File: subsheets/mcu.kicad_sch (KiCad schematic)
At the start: 16 parts, among them U3 LoRa-E5

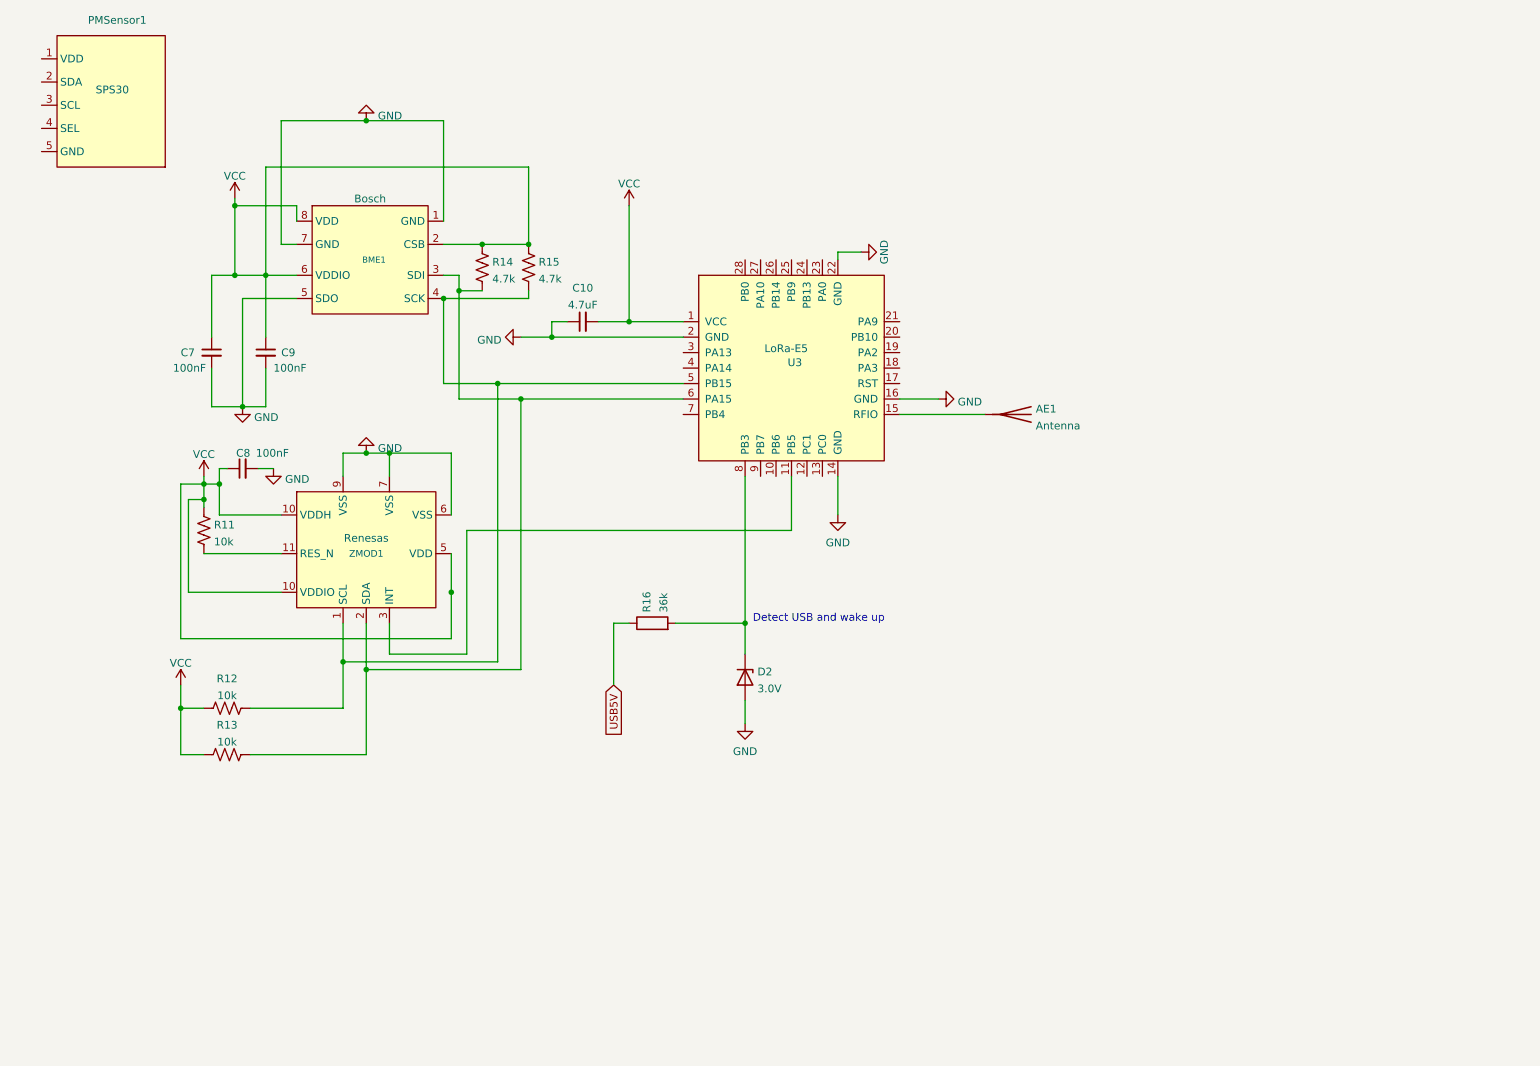
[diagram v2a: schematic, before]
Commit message: USB Comm Interface complete; Sensor and MCU connection complete;
-
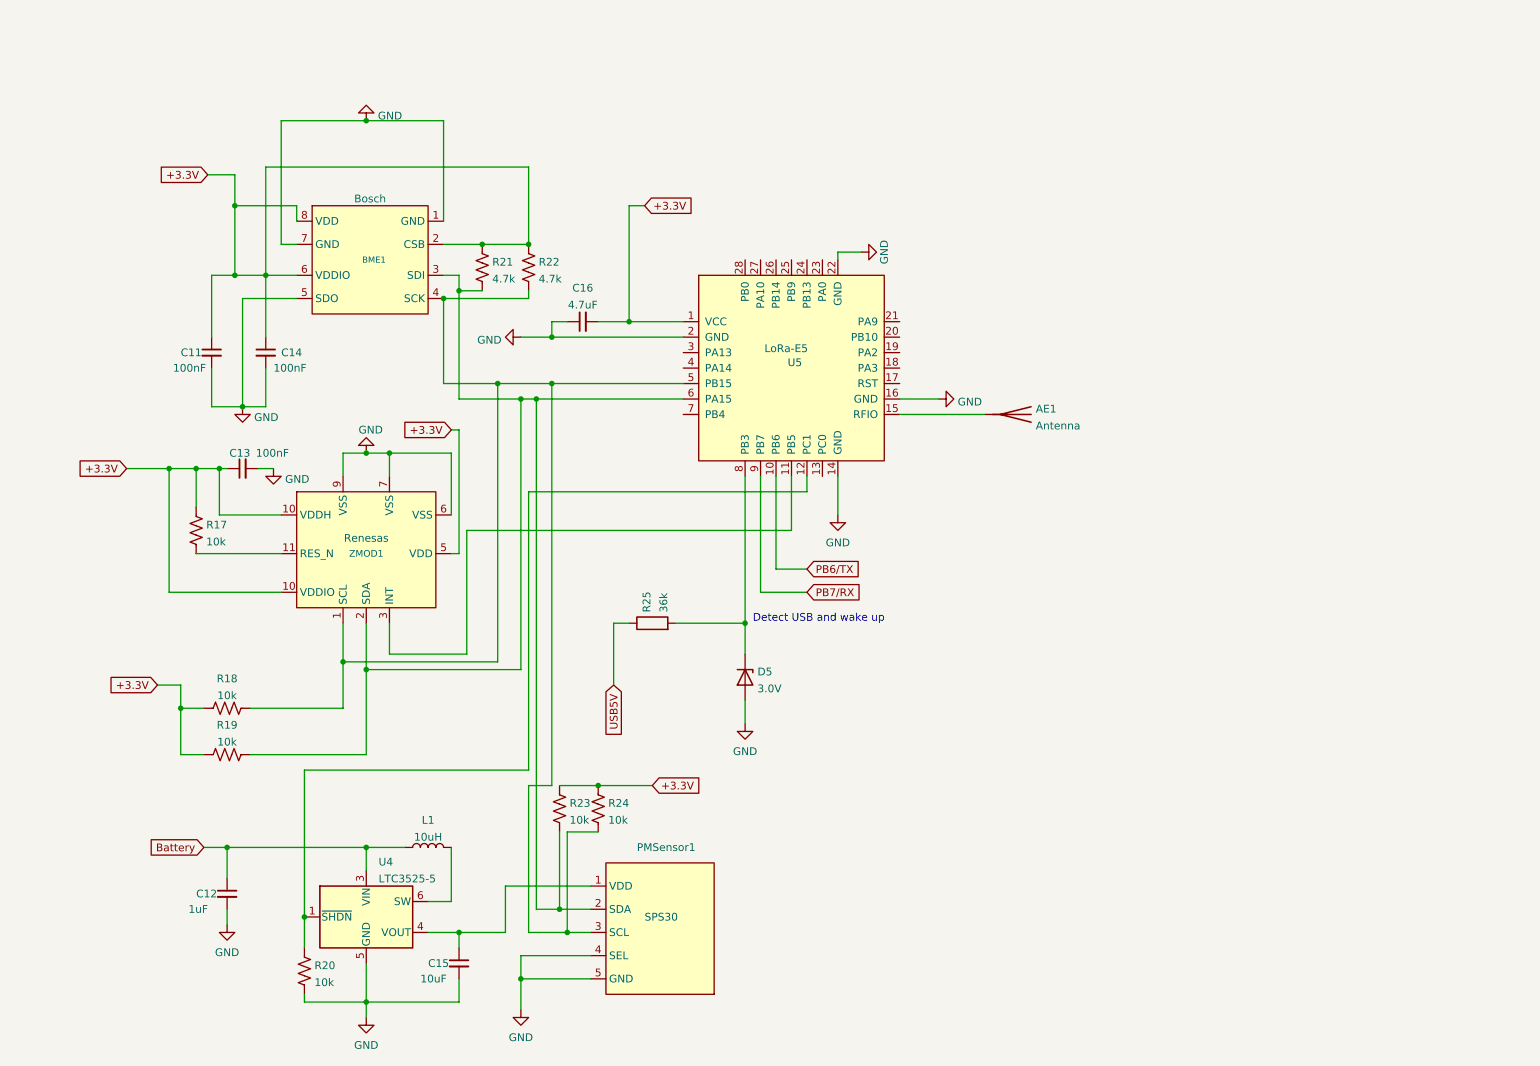
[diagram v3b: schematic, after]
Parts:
- added C12: 1uF, symbol Device:C_Small
- added C15: 10uF, symbol Device:C_Small
- added L1: 10uH, symbol Device:L
- added R20, R23, R24: 10k, symbol Device:R_US
- added U4: LTC3525-5, Package_TO_SOT_SMD:SOT-363_SC-70-6, symbol Regulator_Switching:LTC3525-5
- renumbered C7 to C11, C8 to C13, C9 to C14, C10 to C16, D2 to D5, R11 to R17, R12 to R18, R13 to R19, R14 to R21, R15 to R22, R16 to R25, U3 to U5
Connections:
- net GND: now also PMSensor1.4 (SEL), PMSensor1.5 (GND), C12.2, C15.2, R20.2, U4.2 (GND), U4.5 (GND)
- net PB6/TX: now reaches U5.10 (PB6)
- net at U5.12 (PC1): now also R20.1, U4.1 (~{SHDN})
- net at BME1.4 (SCK), R18.2, R22.2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: now also PMSensor1.3 (SCL), R24.2
- net at BME1.3 (SDI), R19.2, R21.2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: now also PMSensor1.2 (SDA), R23.2
- net PB7/RX: now reaches U5.9 (PB7)
- net at PMSensor1.1 (VDD): now also C15.1, U4.4 (VOUT)
- net VCC renamed +3.3V
- net +3.3V: now also R23.1, R24.1; no longer ZMOD1.n.c (4)
- new net: L1.2, U4.6 (SW)
- new net Battery: C12.1, L1.1, U4.3 (VIN)
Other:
- moved on the sheet: PMSensor1, R17

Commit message: A few schematic changes and fixes
-
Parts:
- removed C12: 1uF, symbol Device:C_Small
- removed C15: 10uF, symbol Device:C_Small
- removed L1: 10uH, symbol Device:L
- removed R20: 10k, symbol Device:R_US
- removed U4: LTC3525-5, Package_TO_SOT_SMD:SOT-363_SC-70-6, symbol Regulator_Switching:LTC3525-5
- renumbered C11 to C13, C13 to C14, C14 to C15, R17 to R18, R18 to R19, R19 to R20
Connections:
- net Boost SHDN/PC1: now reaches U5.12 (PC1)
- net Charge/LBO : now reaches U5.13 (PC0)
- net Charge Done: now reaches U5.20 (PB10)
- net Power On: now reaches U5.21 (PA9)
- net +5V: now reaches PMSensor1.1 (VDD)
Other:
- moved on the sheet: AE1, BME1, C13, C14, C15, C16, D5, PMSensor1, R18, R19, R20, R21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

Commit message: -
-
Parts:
- BME688: renamed from BME1; footprint Package_LGA:LGA-12_2x2mm_P0.5mm -> Package_LGA:Bosch_LGA-8_3x3mm_P0.8mm_ClockwisePinNumbering
- PMSensor1: footprint (none) -> Connector_JST:JST_EH_B5B-EH-A_1x05_P2.50mm_Vertical
- U5: footprint (none) -> LoRa-E5:LoRa-E5
- renumbered ZMOD1 to ZMOD4510

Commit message: USB updated. All footprints added for the most part
-
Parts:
- C13, C14, C15, C16: footprint (none) -> Capacitor_SMD:C_0805_2012Metric_Pad1.18x1.45mm_HandSolder
- R18, R19, R20, R21, R22, R23, R24, R25: footprint (none) -> Resistor_SMD:R_0805_2012Metric_Pad1.20x1.40mm_HandSolder

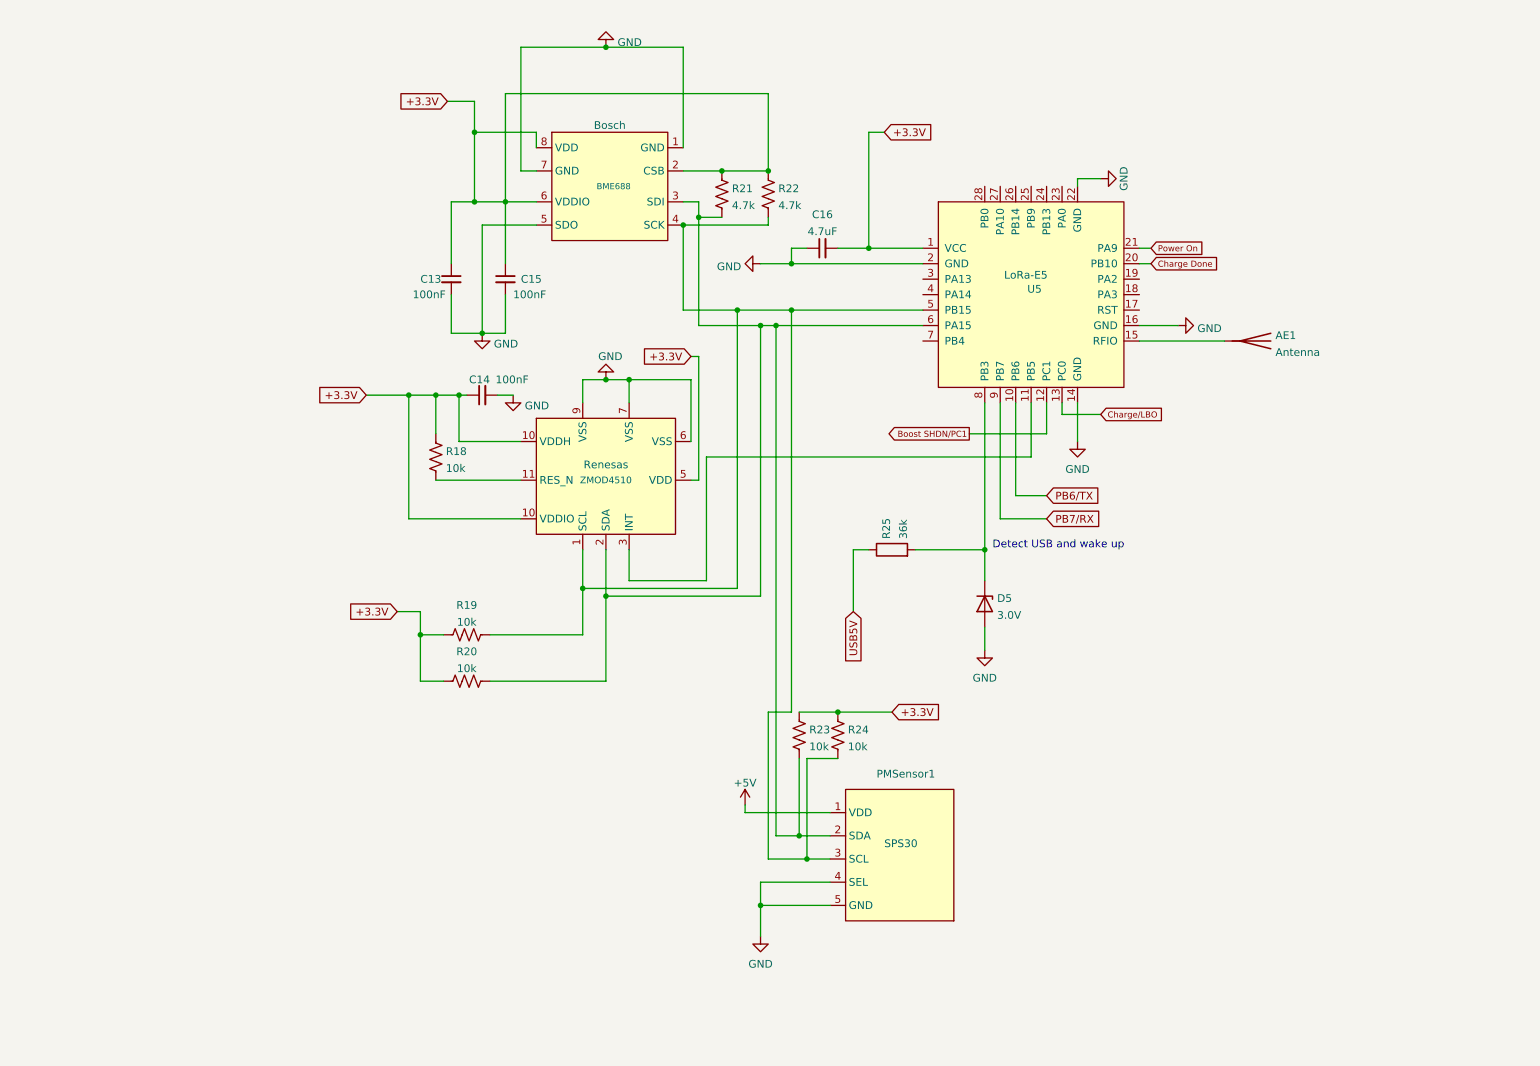
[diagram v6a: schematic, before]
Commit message: Some schematic changes. Preliminary PCB layout complete, routing not done yet
-
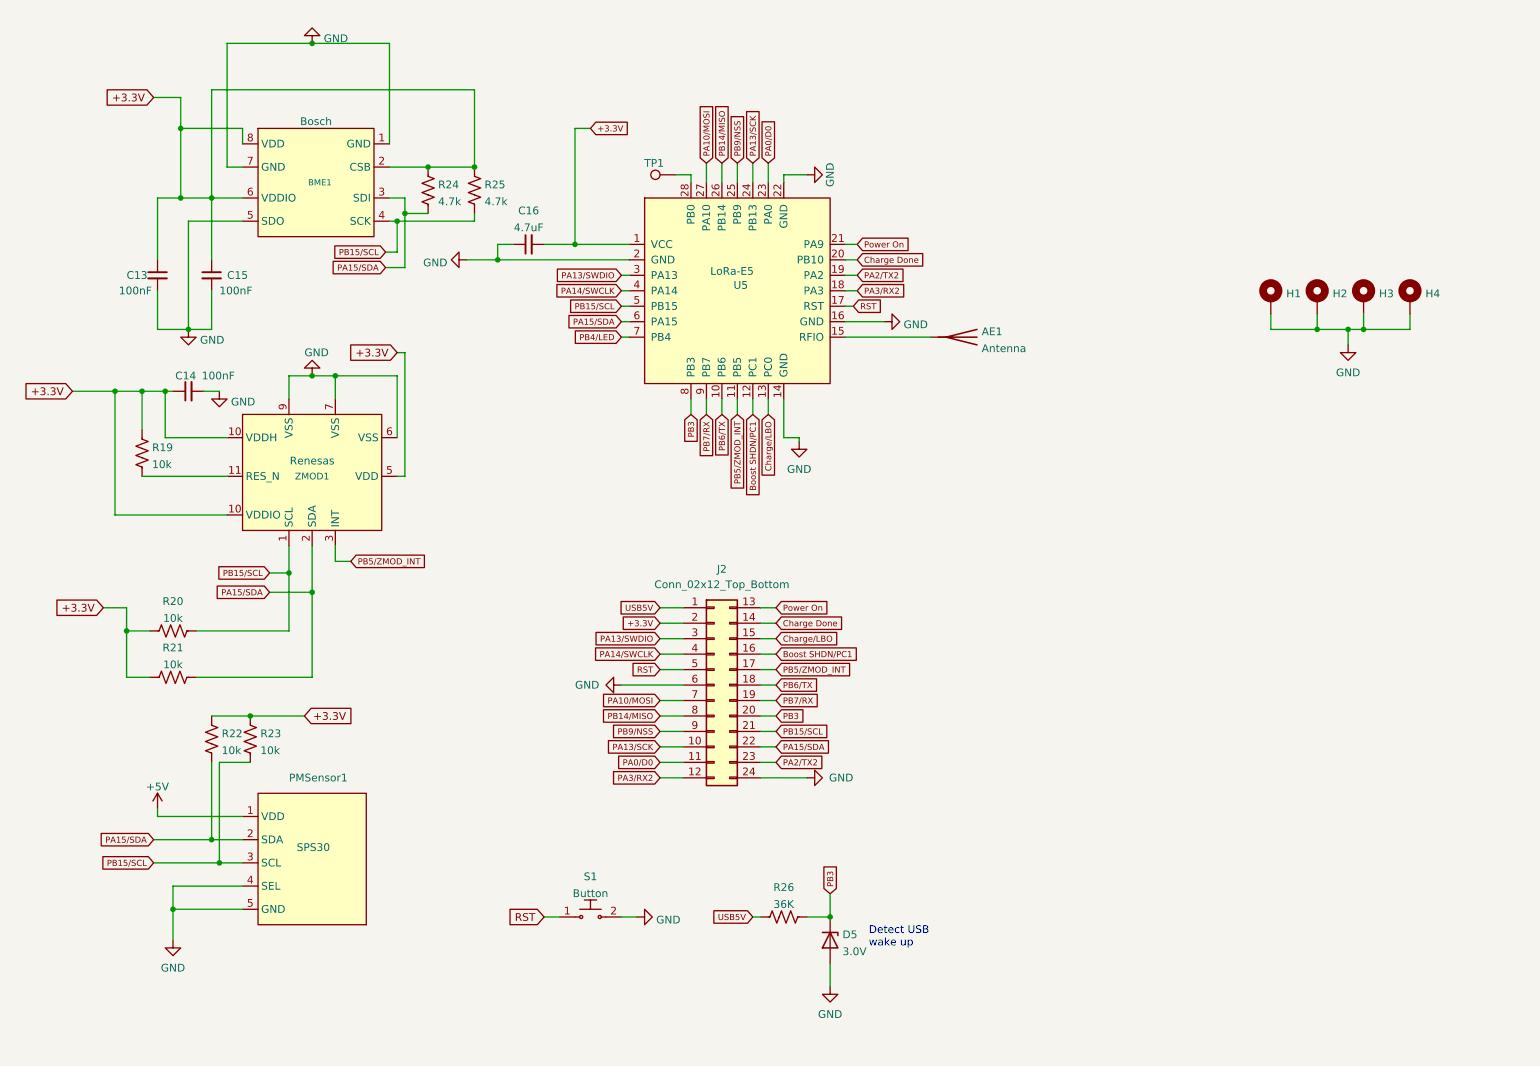
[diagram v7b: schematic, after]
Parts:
- removed R25: 36k, Resistor_SMD:R_0805_2012Metric_Pad1.20x1.40mm_HandSolder, symbol Device:R
- added H1, H2, H3, H4: MountingHole, MountingHole:MountingHole_2.2mm_M2_ISO14580_Pad_TopBottom, symbol Mechanical:MountingHole_Pad
- added J2: Conn_02x12_Top_Bottom, Connector_PinHeader_2.54mm:PinHeader_2x12_P2.54mm_Vertical, symbol Connector_Generic:Conn_02x12_Top_Bottom
- added R26: 36K, Resistor_SMD:R_0805_2012Metric_Pad1.20x1.40mm_HandSolder, symbol Device:R_US
- added S1: Button, Button_Switch_SMD:SW_Push_1P1T_NO_6x6mm_H9.5mm, symbol dk_Pushbutton-Switches:GPTS203211B
- added TP1: TestPoint, TestPoint:TestPoint_Keystone_5005-5009_Compact, symbol Connector:TestPoint
- AE1: footprint (none) -> Connector_Coaxial:SMA_Amphenol_132289_EdgeMount
- D5: footprint (none) -> Diode_SMD:D_0805_2012Metric_Pad1.15x1.40mm_HandSolder
- renumbered BME688 to BME1, R18 to R19, R19 to R20, R20 to R21, R23 to R22, R24 to R23, R21 to R24, R22 to R25, ZMOD4510 to ZMOD1
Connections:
- net +3.3V: now also J2.2 (Pin_2)
- net Boost SHDN/PC1: now also J2.16 (Pin_16)
- net Charge Done: now also J2.14 (Pin_14)
- net Charge/LBO : now also J2.15 (Pin_15)
- net GND: now also H1.1, H2.1, H3.1, H4.1, J2.24 (Pin_24), J2.6 (Pin_6), S1.2
- net PB6/TX: now also J2.18 (Pin_18)
- net PB7/RX: now also J2.19 (Pin_19)
- net Power On: now also J2.13 (Pin_13)
- net USB5V: now also J2.1 (Pin_1), R26.1
- net PB5/ZMOD_INT: now reaches U5.11 (PB5), ZMOD1.3 (INT)
- net PB5/ZMOD_INT: now also J2.17 (Pin_17)
- net RST: now reaches U5.17 (RST)
- net RST: now also J2.5 (Pin_5), S1.1
- net PA3/RX2: now reaches U5.18 (PA3)
- net PA3/RX2: now also J2.12 (Pin_12)
- net PA2/TX2: now reaches U5.19 (PA2)
- net PA2/TX2: now also J2.23 (Pin_23)
- net PA0/D0: now reaches U5.23 (PA0)
- net PA0/D0: now also J2.11 (Pin_11)
- net PA13/SCK: now reaches U5.24 (PB13~{})
- net PA13/SCK: now also J2.10 (Pin_10)
- net PB9/NSS: now reaches U5.25 (PB9)
- net PB9/NSS: now also J2.9 (Pin_9)
- net PB14/MISO: now reaches U5.26 (PB14)
- net PB14/MISO: now also J2.8 (Pin_8)
- net PA10/MOSI: now reaches U5.27 (PA10)
- net PA10/MOSI: now also J2.7 (Pin_7)
- net at U5.28 (PB0): now also TP1.1
- net PA13/SWDIO: now reaches U5.3 (PA13)
- net PA13/SWDIO: now also J2.3 (Pin_3)
- net PA14/SWCLK: now reaches U5.4 (PA14)
- net PA14/SWCLK: now also J2.4 (Pin_4)
- net PB15/SCL: now reaches BME1.4 (SCK), PMSensor1.3 (SCL), R20.2, R23.2, R25.2, U5.5 (PB15), ZMOD1.1 (SCL)
- net PB15/SCL: now also J2.21 (Pin_21)
- net PA15/SDA: now reaches BME1.3 (SDI), PMSensor1.2 (SDA), R21.2, R22.2, R24.2, U5.6 (PA15), ZMOD1.2 (SDA)
- net PA15/SDA: now also J2.22 (Pin_22)
- net PB4/LED: now reaches U5.7 (PB4)
- net PB3: now reaches D5.1 (K), U5.8 (PB3)
- net PB3: now also J2.20 (Pin_20), R26.2
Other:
- note added: "Detect USB wake up"
- note removed: "Detect USB and wake up"
- moved on the sheet: AE1, BME1, C13, C14, C15, C16, D5, PMSensor1, R19, R20, R21, R22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

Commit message: Generated more 3d models for pcb
-
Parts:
- AE1: footprint Connector_Coaxial:SMA_Amphenol_132289_EdgeMount -> Connector_Coaxial:SMA_Amphenol_132134_Vertical
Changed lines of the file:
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@@
       (effects (font (size 1.27 1.27)) (justify left))
     )
-    (property "Footprint" "Connector_Coaxial:SMA_Amphenol_132289_EdgeMount" (id 2) (at 172.72 71.12 0)
+    (property "Footprint" "Connector_Coaxial:SMA_Amphenol_132134_Vertical" (id 2) (at 172.72 71.12 0)
       (effects (font (size 1.27 1.27)) hide)
     )
